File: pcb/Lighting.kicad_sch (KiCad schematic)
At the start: 4 parts, among them U7 TXS0101DBV, U8 TXS0101DBV

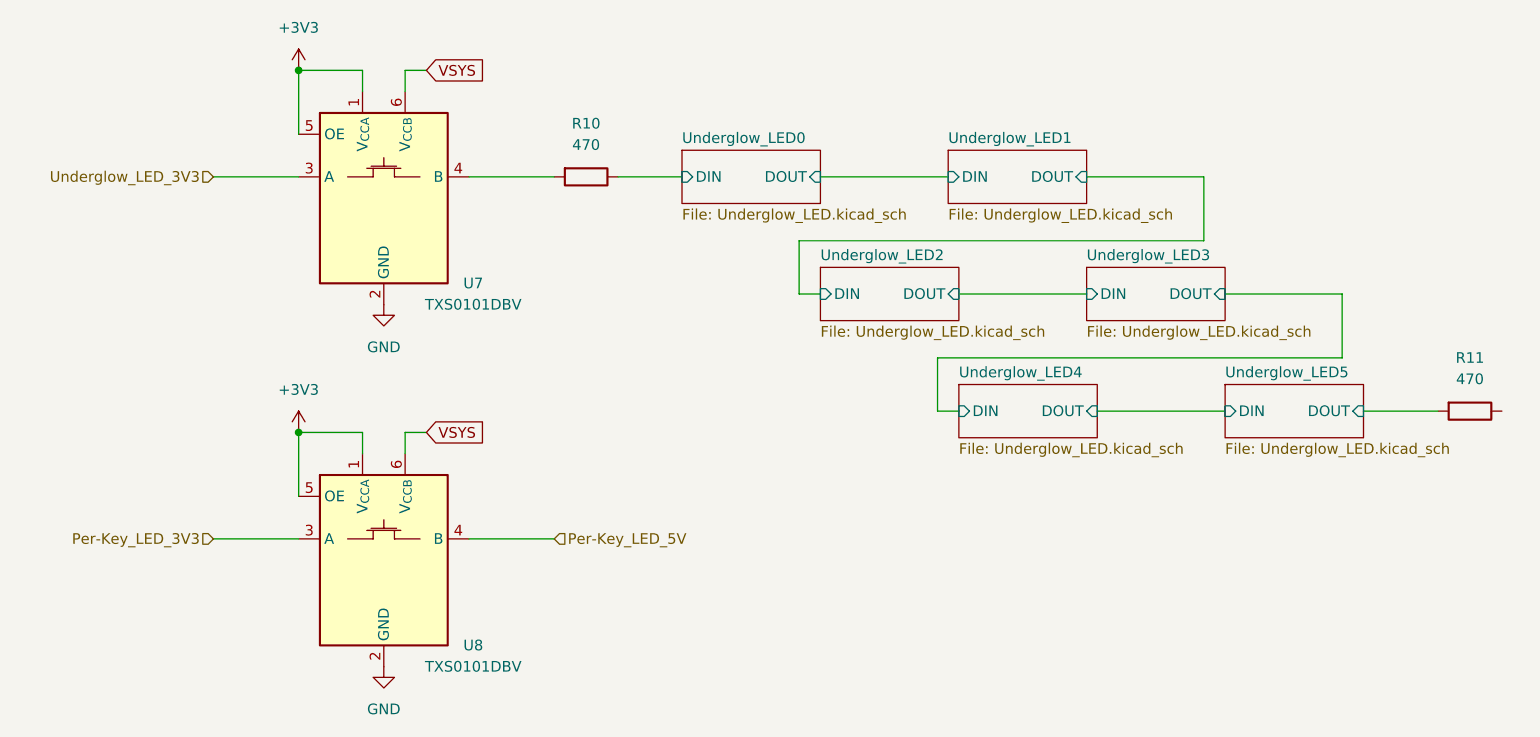
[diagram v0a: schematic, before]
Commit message: Renumbering all reference designations and adding an initial layout for each keyswtich sub-pcb.
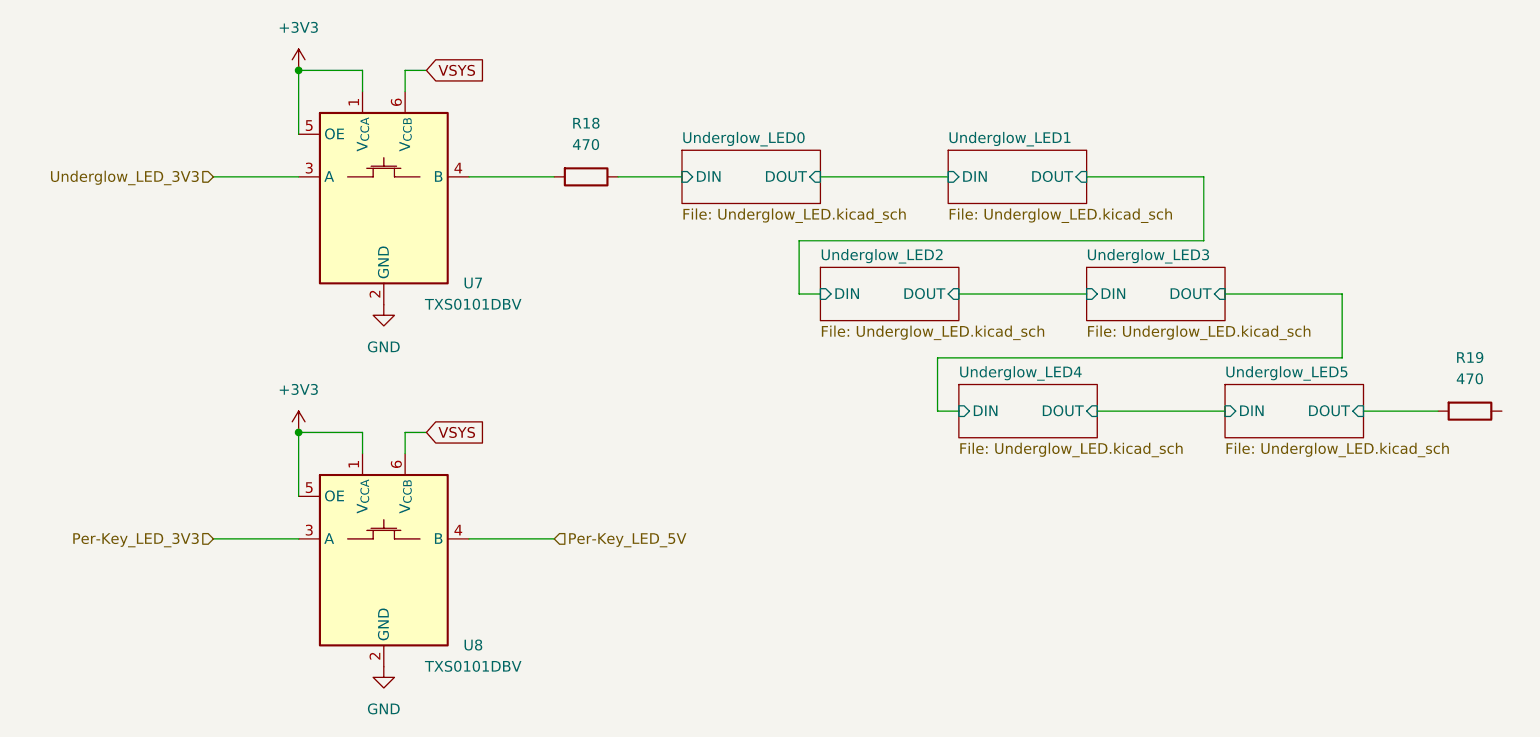
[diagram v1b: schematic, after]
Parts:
- renumbered R10 to R18, R11 to R19
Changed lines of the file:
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@@
 		(dnp no)
 		(fields_autoplaced yes)
-		(property "Reference" "R11"
+		(property "Reference" "R19"
 			(at 194.31 71.12 90)
 			(effects
@@
 			(project "cheapino"
 				(path "/9203b006-47ac-4f34-8cc4-2b709e3df56f/23d46689-c88a-4d8a-9ead-5dd5573c8b8b"
-					(reference "R11")
+					(reference "R19")
 					(unit 1)
 				)
@@
 		(dnp no)
 		(fields_autoplaced yes)
-		(property "Reference" "R10"
+		(property "Reference" "R18"
 			(at 88.9 43.18 90)
 			(effects
@@
 			(project "cheapino"
 				(path "/9203b006-47ac-4f34-8cc4-2b709e3df56f/23d46689-c88a-4d8a-9ead-5dd5573c8b8b"
-					(reference "R10")
+					(reference "R18")
 					(unit 1)
 				)
